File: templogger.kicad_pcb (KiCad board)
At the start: 2 copper layers, 18 parts, among them J1 USB_A, J2 Conn_01x03, U1 MCP2221, U2 ATtiny3216-S, U3 LM35-LP, U4 SC39_11_RT, U5 SC39_11_RT

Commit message: First PCB Layout
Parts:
- moved C5 52.9 mm to (106.6, 47.0)
- moved U3 47.7 mm to (97.8, 26.7), turned to 0 degrees
- moved C2 40.8 mm to (59.1, 34.3), turned to 270 degrees
- moved R1 36.2 mm to (67.3, 41.9), turned to 270 degrees
- moved R2 33.7 mm to (94.0, 46.4), turned to 180 degrees
- moved J2 32.2 mm to (101.6, 50.8)
- moved D1 32.2 mm to (67.3, 36.8), turned to 90 degrees
- moved J1 28.6 mm to (41.3, 30.5)
- moved D2 27.4 mm to (87.0, 46.4), turned to 180 degrees
- moved C1 25.6 mm to (51.4, 34.3), turned to 270 degrees
- moved R4 17.9 mm to (114.9, 29.2)
- moved C3 16.5 mm to (80.8, 28.4)
- moved C4 16.5 mm to (87.0, 23.5)
- moved R3 16.5 mm to (114.9, 37.5)
- moved U2 16.5 mm to (104.1, 37.5)
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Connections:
- U2 pad 10: Net-(U2-Pad10) -> ADC
- U2 pad 3: ADC -> Net-(U2-Pad3)
- U2 pad 4: Seg_2 -> Net-(U2-Pad4)
- U2 pad 5: Seg_DP -> Net-(U2-Pad5)
- U2 pad 6: Net-(U2-Pad6) -> Seg_2
- U2 pad 7: Net-(U2-Pad7) -> Seg_DP
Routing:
- net GND: track 40.9 -> 174.1 mm
- net +5V: track 13.7 -> 134.1 mm
- net Net-(J1-Pad2): track 9.81 -> 51.6 mm
- net Net-(J1-Pad3): track 12.0 -> 47.5 mm
- net Seg_DP: track 50.4 -> 77.7 mm
- net Net-(R4-Pad2): track 18.9 -> 43.3 mm
- net Seg_2: track 44.8 -> 21.6 mm
- net LED: track 0.00 -> 7.51 mm
- net ADC: track 0.00 -> 6.40 mm
- net DAT: track 22.2 -> 16.4 mm
- net Net-(D1-Pad1): track 0.00 -> 5.08 mm
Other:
- board outline added: 109.2 x 33 mm

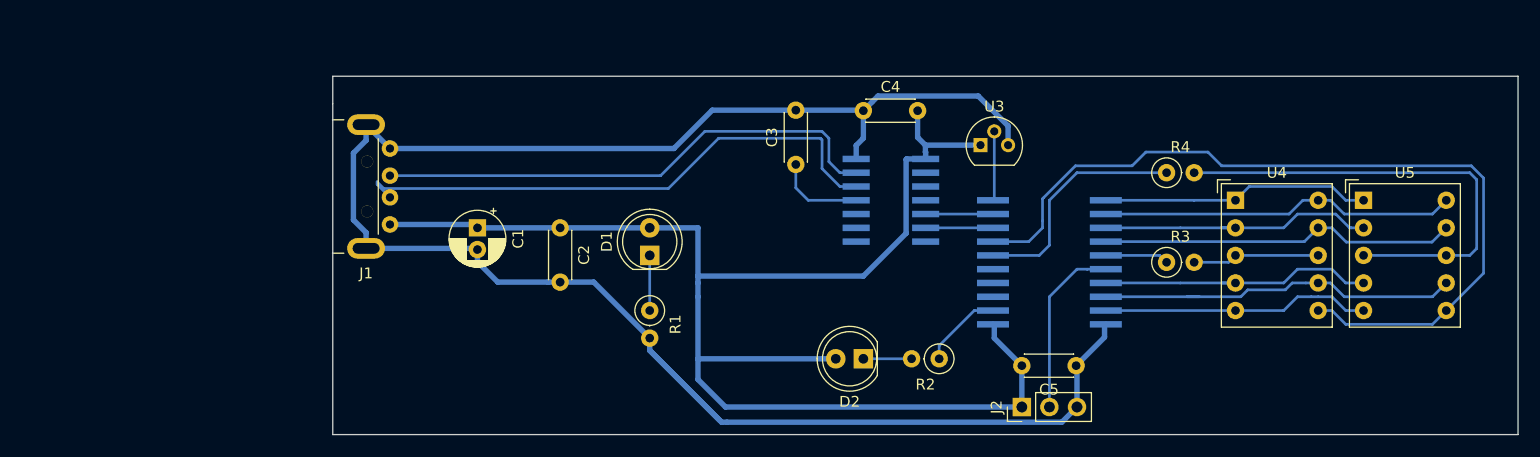
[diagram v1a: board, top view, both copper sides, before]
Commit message: Optimize routing. not done...
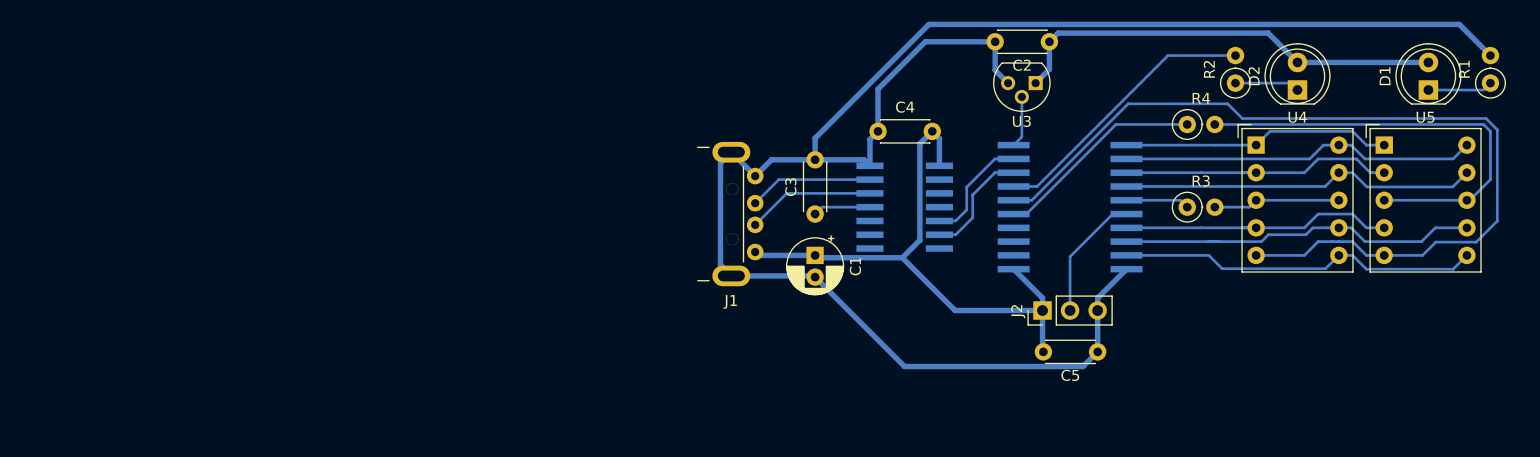
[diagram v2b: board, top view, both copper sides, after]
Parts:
- moved R1 80.3 mm to (144.8, 21.0), turned to 90 degrees
- moved D1 73.4 mm to (139.1, 21.6)
- moved C2 48.2 mm to (104.1, 17.1), turned to 180 degrees
- moved D2 47.1 mm to (127.0, 21.6), turned to 90 degrees
- moved R2 37.3 mm to (121.3, 21.0), turned to 90 degrees
- moved J1 33.8 mm to (74.9, 33.0)
- moved C1 31.2 mm to (82.5, 36.8)
- moved J2 9.09 mm to (103.5, 41.9)
- moved U3 7.65 mm to (102.9, 21.0), turned to 180 degrees
- moved R3 5.43 mm to (116.8, 32.4)
- moved U2 5.43 mm to (106.0, 32.4)
- moved U4 5.43 mm to (123.2, 26.7)
- moved U5 5.43 mm to (135.0, 26.7)
- moved C3 4.91 mm to (82.5, 33.0)
- moved R4 4.84 mm to (116.8, 24.8)
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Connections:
- R2 pad 1: LED -> Net-(D2-Pad1)
- R2 pad 2: Net-(D2-Pad1) -> LED
- U2 pad 19: Seg_D -> Seg_DP
- U2 pad 2: LED -> Net-(U2-Pad2)
- U2 pad 5: Net-(U2-Pad5) -> Seg_2
- U2 pad 6: Seg_2 -> Seg_D
- U2 pad 7: Seg_DP -> LED
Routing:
- net Seg_D: track 25.3 -> 83.5 mm
- net Seg_DP: track 77.7 -> 33.9 mm
- net Net-(J1-Pad2): track 51.6 -> 11.8 mm
- net +5V: track 134.1 -> 94.4 mm
- net Net-(J1-Pad3): track 47.5 -> 11.5 mm
- net LED: track 7.51 -> 25.4 mm
- net GND: track 174.1 -> 168.4 mm
- net DAT: track 16.4 -> 11.8 mm
- net Net-(U1-Pad6): track 6.20 -> 10.4 mm
- net Net-(U1-Pad5): track 6.20 -> 10.4 mm
- net +3V3: track 8.20 -> 5.32 mm
- net Net-(R4-Pad2): track 43.3 -> 40.7 mm
- net Seg_2: track 21.6 -> 19.4 mm
- net ADC: track 6.40 -> 4.76 mm
- net Net-(D2-Pad1): track 4.44 -> 5.98 mm
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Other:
- board outline removed
